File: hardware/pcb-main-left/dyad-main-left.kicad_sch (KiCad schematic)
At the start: 65 parts, among them SW1 SW_Push, SW10 SW_Push, SW11 SW_Push, SW12 SW_Push, SW13 SW_Push, SW14 SW_Push, SW15 SW_Push, SW16 SW_Push, SW17 SW_Push, SW18 SW_Push, SW19 SW_Push, SW2 SW_Push, SW20 SW_Push, SW21 SW_Push, SW22 SW_Push, SW23 SW_Push, SW24 SW_Push, SW25 SW_Push, SW26 SW_Push, SW27 SW_Push, SW28 SW_Push, SW29 SW_Push, SW3 SW_Push, SW30 SW_Push, SW31 SW_Push, SW32 SW_Push, SW4 SW_Push, SW5 SW_Push, SW6 SW_Push, SW7 SW_Push, SW8 SW_Push, SW9 SW_Push

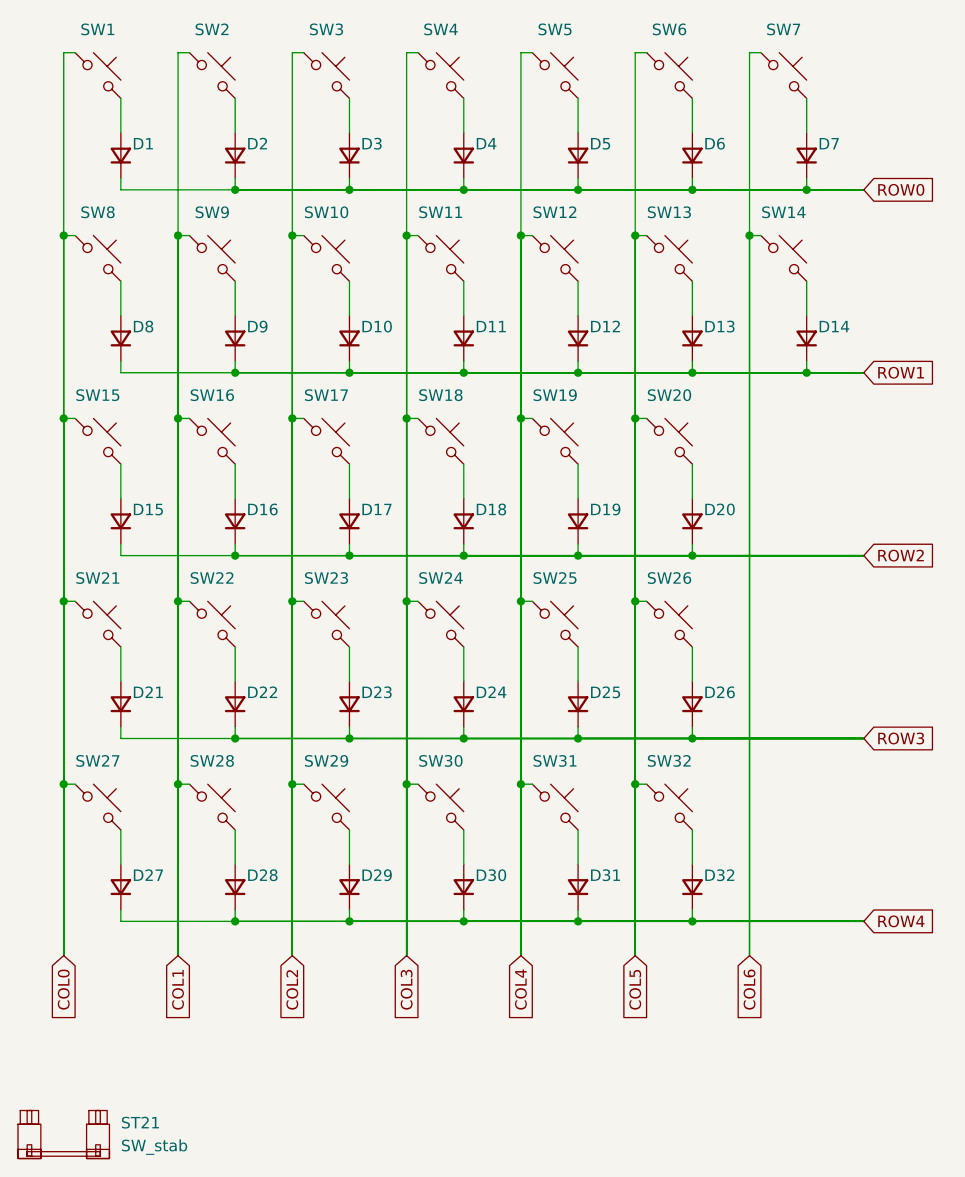
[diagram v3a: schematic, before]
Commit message: Regenerate both main PCBs with hierarchical sheet bundling
Re-ran generate_main_pcbs.py so the --bundle-strategy hierarchical change
takes effect. Each half now has a proper root sheet:

  dyad-main-<half>.kicad_sch             0 symbols, 2 child sheet refs
  dyad-main-<half>-key-matrix.kicad_sch  65 / 74 symbols   (new file)
  dyad-main-<half>-led-chain.kicad_sch   130 / 150 symbols

The key-matrix sheet is new: flat bundling put those symbols in the root
itself, hierarchical moves them into their own child sheet.

Schematic parity is the point of the exercise:

              before              after
  main-left   64 Extra footprint  0
  main-right  74 Extra footprint  0

Every LED and decoupling capacitor now resolves to a symbol. The parity
counts happen to be unchanged (98 and 111) but the composition is entirely
different -- what remains is cosmetic field sync (Sim.Device, Description
and Datasheet empty on the PCB side), not missing structure.

min_copper_edge_clearance is 0.2 on both, so _relax_edge_clearance ran, and
the fp-lib-table files added earlier were preserved, so lib_footprint_issues
stays at zero.

Known, unchanged by this commit:
  - COL6 vs LED14's cutout is back at 0.036 mm on main-right, identical to
    before -- kbplacer re-routes it the same way every time, which is why
    the hand fix in e7043c7 was always going to be temporary.
  - The 2.25u stabilised key still falls back to a 1.0u footprint.
  - Four rotated thumb/pod pairs per half remain unrouted ("Could not route
    pads when parent footprints not rotated the same").

Co-Authored-By: Claude Opus 5 <noreply@anthropic.com>
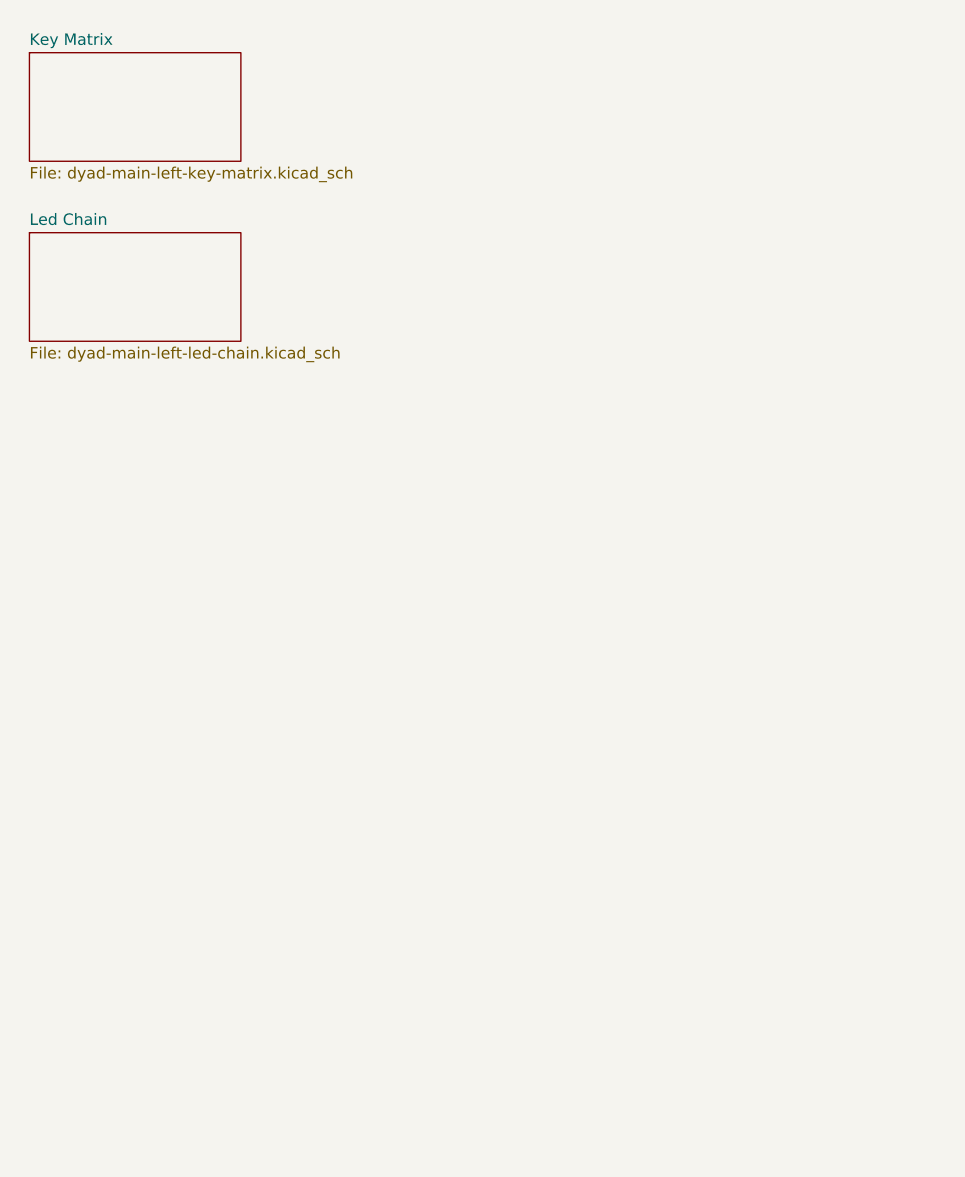
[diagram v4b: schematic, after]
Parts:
- removed D1, D10, D11, D12, D13, D14, D15, D16, D17, D18, D19, D2, D20, D21, D22, D23, D24, D25, D26, D27, D28, D29, D3, D30, D31, D32, D4, D5, D6, D7, D8, D9: D, Diode_SMD:D_SOD-123, symbol Device:D_Small
- removed ST21: SW_stab, marbastlib-mx:STAB_MX_2.25u, symbol Mechanical:SW_stab
- removed SW1, SW10, SW11, SW12, SW13, SW14, SW16, SW17, SW18, SW19, SW2, SW20, SW21, SW22, SW23, SW24, SW25, SW26, SW27, SW28, SW3, SW31, SW4, SW5, SW6, SW7, SW9: SW_Push, marbastlib-mx:SW_MX_HS_CPG151101S11_1u, symbol Switch:SW_Push_45deg
- removed SW15: SW_Push, marbastlib-mx:SW_MX_HS_CPG151101S11_1.75u, symbol Switch:SW_Push_45deg
- removed SW29, SW30: SW_Push, marbastlib-mx:SW_MX_HS_CPG151101S11_1.25u, symbol Switch:SW_Push_45deg
- removed SW32, SW8: SW_Push, marbastlib-mx:SW_MX_HS_CPG151101S11_1.5u, symbol Switch:SW_Push_45deg
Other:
- added sheet Key Matrix (dyad-main-left-key-matrix.kicad_sch)
- added sheet Led Chain (dyad-main-left-led-chain.kicad_sch)
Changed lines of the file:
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@@
+(kicad_sch
+    (version 20250114)
+    (generator "eeschema")
+    (generator_version "9.0")
+    (paper "A4")
+    (sheet
+        (at 21.59 20.32)
+        (size 23.495 12.065)
+        (exclude_from_sim no)
+        (in_bom yes)
+        (on_board yes)
+        (dnp no)
+        (fields_autoplaced yes)
+        (stroke
+            (width 0.1524)
+            (type solid)
+        )
+        (fill
+            (color 0 0 0 0)
+        )
+        (property "Sheetname" "Key Matrix"
+            (at 21.59 19.6084 0)
+            (show_name no)
+            (do_not_autoplace no)
+            (effects
+                (font
+                    (size 1.27 1.27)
+                )
+                (justify left bottom)
+            )
+        )
+        (property "Sheetfile" "dyad-main-left-key-matrix.kicad_sch"
+            (at 21.59 32.9696 0)
+            (show_name no)
+            (do_not_autoplace no)
+            (effects
+                (font
+                    (size 1.27 1.27)
+                )
+                (justify left top)
+            )
+        )
+        (instances
+            (project "dyad-main-left"
+                (path "/d859e60a-10d9-4f56-b778-fa81b487a1fc"
+                    (page "2")
+                )
+            )
+        )
+    )
+    (sheet
+        (at 21.59 40.32)
+        (size 23.495 12.065)
+        (exclude_from_sim no)
+        (in_bom yes)
+        (on_board yes)
+        (dnp no)
+        (fields_autoplaced yes)
+        (stroke
+            (width 0.1524)
+            (type solid)
+        )
+        (fill
+            (color 0 0 0 0)
+        )
+        (property "Sheetname" "Led Chain"
+            (at 21.59 39.6084 0)
+            (show_name no)
+            (do_not_autoplace no)
+            (effects
+                (font
+                    (size 1.27 1.27)
+                )
+                (justify left bottom)
+            )
+        )
+        (property "Sheetfile" "dyad-main-left-led-chain.kicad_sch"
+            (at 21.59 52.9696 0)
+            (show_name no)
+            (do_not_autoplace no)
+            (effects
+                (font
+                    (size 1.27 1.27)
+                )
+                (justify left top)
+            )
+        )
+        (instances
+            (project "dyad-main-left"
+                (path "/d859e60a-10d9-4f56-b778-fa81b487a1fc"
+                    (page "3")
+                )
+            )
+        )
+    )
+    (sheet_instances
+        (path "/"
+            (page "1")
+        )
+    )
+    (embedded_fonts no)
+)
